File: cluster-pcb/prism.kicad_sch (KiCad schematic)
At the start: 8 parts, among them J501 FFC_P1mm_BOT_RA_SMD, U501 MAX13431E

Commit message: Update to version 1.1
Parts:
- removed D501: D_Zener_47V_1W, Janelia:D_SMA, symbol Janelia:D_Zener_47V_1W
- removed D502: D, Janelia:D_SMB, symbol Janelia:D_1.25V@2A_400V
- removed R501: 0.24, Janelia:R_2512_6332Metric, symbol Janelia:R_0.240_1W_2512
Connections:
- net VCC is gone; now on net VAA: J501.1 (Pin_1), J501.2 (Pin_2), J501.3 (Pin_3), J501.4 (Pin_4)
- net GND: now also U501.7 (NC)
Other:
- note removed: "Convert 48V down to ~46V."

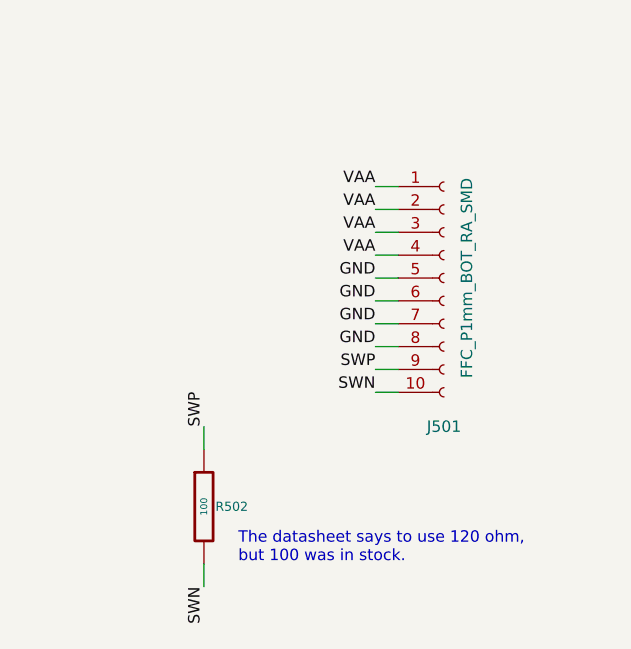
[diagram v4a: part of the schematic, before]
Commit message: 100 -> 120 ohm and change connectors
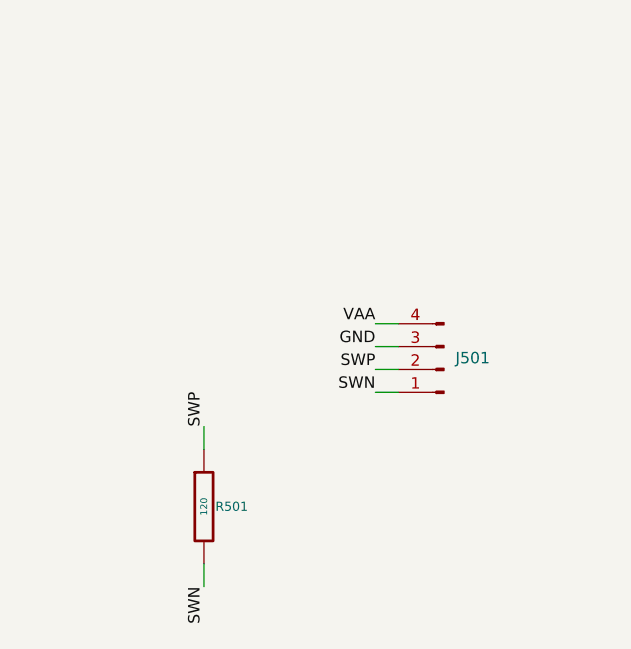
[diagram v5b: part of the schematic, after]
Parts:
- removed J501: FFC_P1mm_BOT_RA_SMD, Janelia:CONN_C2914097, symbol Janelia:Conn_01x10_FFC_P1mm_BOT_RA_SMD
- removed R502: 100, Janelia:R_0402_1005Metric, symbol Janelia:R_100_0402
- added J501: Conn_01x04_P3.5mm_TBH_Horizontal_Screw, Janelia:PhoenixContact_MC_1,5_4-G-3.5_1x04_P3.50mm_Horizontal_Screw, symbol Janelia:Conn_01x04_P3.5mm_TBH_Horizontal_Screw
- added R501: 120, Janelia:R_0402_1005Metric, symbol Janelia:R_120_0402
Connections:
- net GND: now also J501.3 (Pin_3)
- net SWN: now also J501.1 (Pin_1), R501.2
- net SWP: now also J501.2 (Pin_2), R501.1
- net VAA: now also J501.4 (Pin_4)
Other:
- note removed: "The datasheet says to use 120 ohm, but 100 was in stock."
